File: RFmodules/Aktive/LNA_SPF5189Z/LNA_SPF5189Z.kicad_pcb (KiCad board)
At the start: 2 copper layers, 32 x 18 mm, 15 parts, among them J1 SMA, J2 SMA, U1 PSA4-5043+

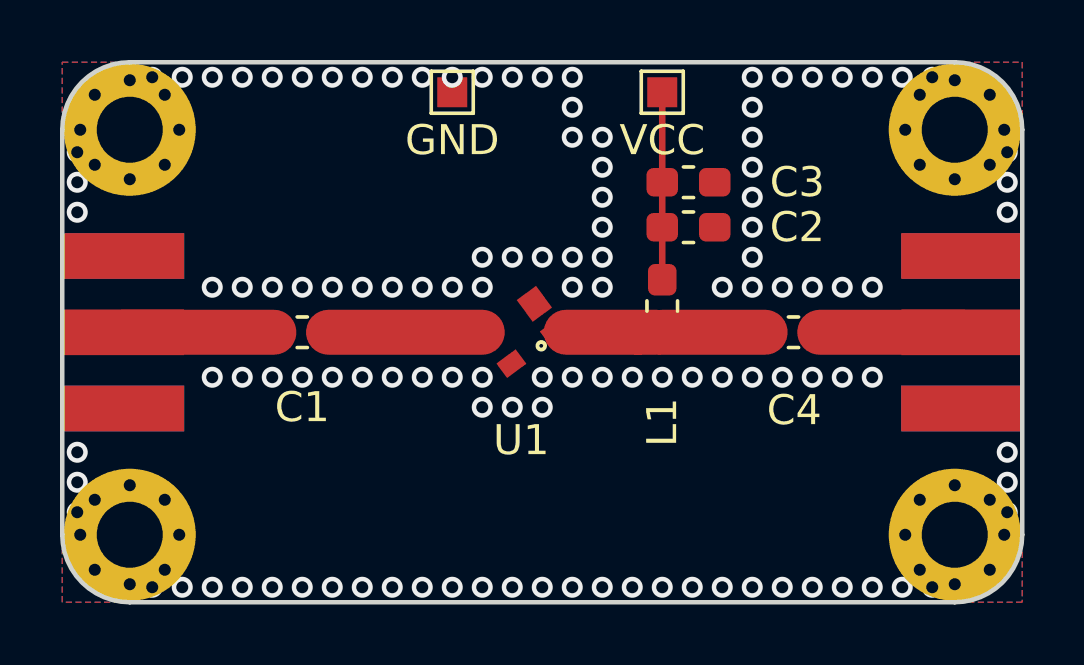
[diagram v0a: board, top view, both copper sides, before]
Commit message: Add LNA SPF5189Z module
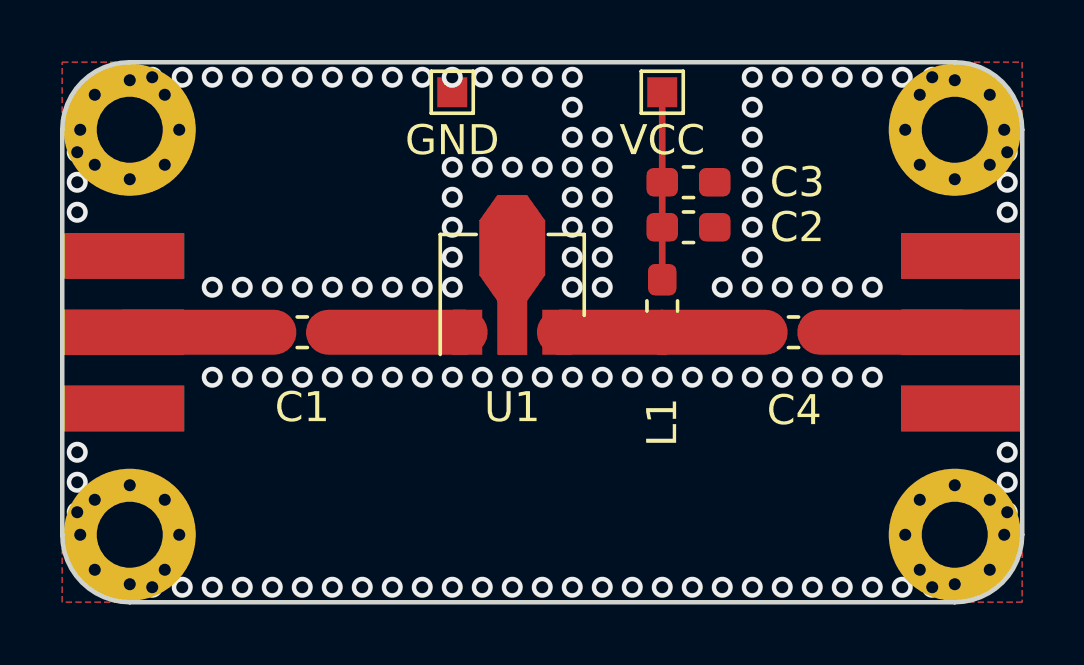
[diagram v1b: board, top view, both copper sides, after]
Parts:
- U1: value PSA4-5043+ -> SPF5189Z; footprint PSA4-5043_:PSA4-5043+ -> Package_TO_SOT_SMD:SOT-89-3
- moved U1 1.50 mm to (115.0, 107.5), turned to 90 degrees
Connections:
- U1 pad 1: Net-(C4-Pad2) -> Net-(C1-Pad1)
- U1 pad 3: Net-(C1-Pad1) -> Net-(C4-Pad2)
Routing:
- net Net-(C1-Pad1): track 5.13 -> 4.55 mm
- net GND: vias 121 -> 125
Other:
- board text added: "SPF5189Z Revision 2 - 02/2019 github.com/fgaletsee/RFLego"
- board text removed: "LNA - PSA4-5043+ Revision 2 - 02/2019 github.com/fgaletsee/RFLego"
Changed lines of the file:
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@@
     (thickness 1.6)
     (drawings 27)
-    (tracks 130)
+    (tracks 133)
     (zones 0)
     (modules 15)
@@
     (pad 1 smd rect (at 0 0) (size 1 1) (layers F.Cu F.Mask)
       (net 4 "Net-(C2-Pad2)"))
-  )
-  (module PSA4-5043_:PSA4-5043+ (layer F.Cu)
-    (at 115.310161 108.989104 126.4)
-    (attr smd)
-    (fp_text reference U1 (at -2.900358 -2.150952) (layer F.SilkS)
-      (effects (font (size 1 1) (thickness 0.15)))
-    )
-    (fp_text value PSA4-5043+ (at -5.353234 -3.710888) (layer F.SilkS) hide
-      (effects (font (size 1 1) (thickness 0.15)))
-    )
-    (fp_line (start -1 -0.549999) (end 0.999999 -0.549999) (layer Dwgs.User) (width 0.2032))
-    (fp_line (start 1 0.549999) (end -0.999999 0.549999) (layer Dwgs.User) (width 0.2032))
-    (fp_poly (pts (xy 0.150171 0.6) (xy 0.85 0.6) (xy 0.85 1.10126) (xy 0.150171 1.10126)) (layer Dwgs.User) (width 0))
-    (fp_poly (pts (xy -0.851089 0.6) (xy -0.45 0.6) (xy -0.45 1.10141) (xy -0.851089 1.10141)) (layer Dwgs.User) (width 0))
-    (fp_poly (pts (xy -0.851105 -1.1) (xy -0.45 -1.1) (xy -0.45 -0.60078) (xy -0.851105 -0.60078)) (layer Dwgs.User) (width 0))
-    (fp_poly (pts (xy 0.450588 -1.1) (xy 0.85 -1.1) (xy 0.85 -0.600784) (xy 0.450588 -0.600784)) (layer Dwgs.User) (width 0))
-    (fp_circle (center -0.762 0.254) (end -0.635 0.254) (layer F.SilkS) (width 0.127))
-    (pad 2 smd rect (at 0.5 0.899999 126.4) (size 0.9 0.8) (layers F.Cu F.Paste F.Mask)
-      (net 1 GND))
-    (pad 1 smd rect (at -0.65 0.9 126.4) (size 0.6 0.8) (layers F.Cu F.Paste F.Mask)
-      (net 5 "Net-(C4-Pad2)"))
-    (pad 4 smd rect (at -0.65 -0.899999 126.4) (size 0.6 0.8) (layers F.Cu F.Paste F.Mask)
-      (net 1 GND))
-    (pad 3 smd rect (at 0.65 -0.9 126.4) (size 0.6 0.8) (layers F.Cu F.Paste F.Mask)
-      (net 2 "Net-(C1-Pad1)"))
   )
   (module Symbol:OSHW-Logo2_9.8x8mm_SilkScreen (layer B.Cu)
@@
       (xy -3.43224 -2.584467) (xy -3.324904 -2.572722) (xy -3.231114 -2.584505)) (layer B.SilkS) (width 0.01))
   )
+  (module Package_TO_SOT_SMD:SOT-89-3 (layer F.Cu)
+    (at 115 107.52 90)
+    (descr SOT-89-3)
+    (tags SOT-89-3)
+    (attr smd)
+    (fp_text reference U1 (at -3.98 0 180) (layer F.SilkS)
+      (effects (font (size 1 1) (thickness 0.15)))
+    )
+    (fp_text value SPF5189Z (at 0.45 3.25 90) (layer F.Fab)
+      (effects (font (size 1 1) (thickness 0.15)))
+    )
+    (fp_text user %R (at 0.38 0 180) (layer F.Fab)
+      (effects (font (size 0.6 0.6) (thickness 0.09)))
+    )
+    (fp_line (start 1.78 1.2) (end 1.78 2.4) (layer F.SilkS) (width 0.12))
+    (fp_line (start 1.78 2.4) (end -0.92 2.4) (layer F.SilkS) (width 0.12))
+    (fp_line (start -2.22 -2.4) (end 1.78 -2.4) (layer F.SilkS) (width 0.12))
+    (fp_line (start 1.78 -2.4) (end 1.78 -1.2) (layer F.SilkS) (width 0.12))
+    (fp_line (start -0.92 -1.51) (end -0.13 -2.3) (layer F.Fab) (width 0.1))
+    (fp_line (start 1.68 -2.3) (end 1.68 2.3) (layer F.Fab) (width 0.1))
+    (fp_line (start 1.68 2.3) (end -0.92 2.3) (layer F.Fab) (width 0.1))
+    (fp_line (start -0.92 2.3) (end -0.92 -1.51) (layer F.Fab) (width 0.1))
+    (fp_line (start -0.13 -2.3) (end 1.68 -2.3) (layer F.Fab) (width 0.1))
+    (fp_line (start 3.23 -2.55) (end 3.23 2.55) (layer F.CrtYd) (width 0.05))
+    (fp_line (start 3.23 -2.55) (end -2.48 -2.55) (layer F.CrtYd) (width 0.05))
+    (fp_line (start -2.48 2.55) (end 3.23 2.55) (layer F.CrtYd) (width 0.05))
+    (fp_line (start -2.48 2.55) (end -2.48 -2.55) (layer F.CrtYd) (width 0.05))
+    (pad 2 smd trapezoid (at 2.667 0) (size 1.6 0.85) (rect_delta 0 0.6 ) (layers F.Cu F.Paste F.Mask)
+      (net 1 GND))
+    (pad 1 smd rect (at -1.48 -1.5) (size 1 1.5) (layers F.Cu F.Paste F.Mask)
+      (net 2 "Net-(C1-Pad1)"))
+    (pad 2 smd rect (at -1.3335 0) (size 1 1.8) (layers F.Cu F.Paste F.Mask)
+      (net 1 GND))
+    (pad 3 smd rect (at -1.48 1.5) (size 1 1.5) (layers F.Cu F.Paste F.Mask)
+      (net 5 "Net-(C4-Pad2)"))
+    (pad 2 smd rect (at 1.3335 0) (size 2.2 1.84) (layers F.Cu F.Paste F.Mask)
+      (net 1 GND))
+    (pad 2 smd trapezoid (at -0.0762 0 180) (size 1.5 1) (rect_delta 0 0.7 ) (layers F.Cu F.Paste F.Mask)
+      (net 1 GND))
+    (model ${KISYS3DMOD}/Package_TO_SOT_SMD.3dshapes/SOT-89-3.wrl
+      (at (xyz 0 0 0))
+      (scale (xyz 1 1 1))
+      (rotate (xyz 0 0 0))
+    )
+  )
   (gr_line (start 102.25 100) (end 117 100) (layer B.Mask) (width 2))
   (gr_line (start 123 100) (end 129.75 100) (layer B.Mask) (width 2))
   (gr_line (start 123 100) (end 129.75 100) (layer F.Mask) (width 2))
-  (gr_text "LNA - PSA4-5043+\nRevision 2 - 02/2019\ngithub.com/fgaletsee/RFLego" (at 127.75 106.25) (layer B.SilkS)
+  (gr_text "SPF5189Z\nRevision 2 - 02/2019\ngithub.com/fgaletsee/RFLego" (at 127.75 106.25) (layer B.SilkS)
     (effects (font (size 1 1) (thickness 0.25)) (justify left mirror))
   )
@@
   (via (at 117 110.5) (size 0.7) (drill 0.4) (layers F.Cu B.Cu) (net 1))
   (via (at 116 110.5) (size 0.7) (drill 0.4) (layers F.Cu B.Cu) (net 1))
-  (via (at 116 111.5) (size 0.7) (drill 0.4) (layers F.Cu B.Cu) (net 1))
-  (via (at 115 111.5) (size 0.7) (drill 0.4) (layers F.Cu B.Cu) (net 1))
-  (via (at 114 111.5) (size 0.7) (drill 0.4) (layers F.Cu B.Cu) (net 1))
   (via (at 113 110.5) (size 0.7) (drill 0.4) (layers F.Cu B.Cu) (net 1))
   (via (at 114 110.5) (size 0.7) (drill 0.4) (layers F.Cu B.Cu) (net 1))
   (via (at 113 107.5) (size 0.7) (drill 0.4) (layers F.Cu B.Cu) (net 1))
-  (via (at 114 107.5) (size 0.7) (drill 0.4) (layers F.Cu B.Cu) (net 1))
-  (via (at 114 106.5) (size 0.7) (drill 0.4) (layers F.Cu B.Cu) (net 1))
-  (via (at 115 106.5) (size 0.7) (drill 0.4) (layers F.Cu B.Cu) (net 1))
-  (via (at 116 106.5) (size 0.7) (drill 0.4) (layers F.Cu B.Cu) (net 1))
-  (via (at 117 106.5) (size 0.7) (drill 0.4) (layers F.Cu B.Cu) (net 1))
   (via (at 117 107.5) (size 0.7) (drill 0.4) (layers F.Cu B.Cu) (net 1))
   (via (at 118 107.5) (size 0.7) (drill 0.4) (layers F.Cu B.Cu) (net 1))
@@
   (via (at 111 110.5) (size 0.7) (drill 0.4) (layers F.Cu B.Cu) (net 1))
   (via (at 112 110.5) (size 0.7) (drill 0.4) (layers F.Cu B.Cu) (net 1))
-  (segment (start 108.875 109) (end 114.000532 109) (width 1.5) (layer F.Cu) (net 2))
+  (via (at 115 110.5) (size 0.7) (drill 0.4) (layers F.Cu B.Cu) (net 1))
+  (via (at 117 106.5) (size 0.7) (drill 0.4) (layers F.Cu B.Cu) (net 1))
+  (via (at 117 105.5) (size 0.7) (drill 0.4) (layers F.Cu B.Cu) (net 1))
+  (via (at 117 104.5) (size 0.7) (drill 0.4) (layers F.Cu B.Cu) (net 1))
+  (via (at 113 106.5) (size 0.7) (drill 0.4) (layers F.Cu B.Cu) (net 1))
+  (via (at 113 105.5) (size 0.7) (drill 0.4) (layers F.Cu B.Cu) (net 1))
+  (via (at 113 104.5) (size 0.7) (drill 0.4) (layers F.Cu B.Cu) (net 1))
+  (via (at 113 103.5) (size 0.7) (drill 0.4) (layers F.Cu B.Cu) (net 1))
+  (via (at 114 103.5) (size 0.7) (drill 0.4) (layers F.Cu B.Cu) (net 1))
+  (via (at 115 103.5) (size 0.7) (drill 0.4) (layers F.Cu B.Cu) (net 1))
+  (via (at 116 103.5) (size 0.7) (drill 0.4) (layers F.Cu B.Cu) (net 1))
+  (via (at 117 103.5) (size 0.7) (drill 0.4) (layers F.Cu B.Cu) (net 1))
+  (segment (start 108.875 109) (end 113.429999 109) (width 1.5) (layer F.Cu) (net 2))
   (segment (start 102.032 109) (end 107.05499 109) (width 1.5) (layer F.Cu) (net 3))
   (segment (start 120 107.25) (end 120 105.5) (width 0.22) (layer F.Cu) (net 4))
   (segment (start 120 105.5) (end 120 104) (width 0.22) (layer F.Cu) (net 4))
   (segment (start 120 104) (end 120 101) (width 0.22) (layer F.Cu) (net 4))
-  (segment (start 119.163924 109) (end 116.8 109) (width 1.5) (layer F.Cu) (net 5))
   (segment (start 120 109) (end 123.42999 109) (width 1.5) (layer F.Cu) (net 5))
-  (segment (start 119.8 109) (end 119.225 109) (width 1.5) (layer F.Cu) (net 5))
+  (segment (start 120 109) (end 116.570001 109) (width 1.5) (layer F.Cu) (net 5))
   (segment (start 130 109) (end 125.25 109) (width 1.5) (layer F.Cu) (net 6))
   (zone (net 1) (net_name GND) (layer F.Cu) (hatch edge 0.508)
